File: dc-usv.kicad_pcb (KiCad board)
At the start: 4 copper layers, 120 x 100 mm, 327 parts, among them J1 Output 2.0mm, J10 I2C, J2 Output 2.0mm, J3 Output 2.0mm, J4 SMBUS, J5 HanRun_HR911105A, J6 USB_C_Receptacle_USB2.0, J7 Input 2.0mm, J8 Input 2.5mm, J9 USB_C_Receptacle_USB2.0, Q1 AON7544, Q10 AO4407A, Q11 2N7002, Q12 MMBT3904, Q13 2N7002, Q14 2N7002, Q15 2N7002, Q16 2N7002, Q17 2N7002, Q18 MMBT3904, Q19 AO4407A, Q2 AO3401A, Q20 2N7002, Q21 AO4407A, Q22 2N7002, Q23 AO4407A, Q24 2N7002, Q25 AO3401A, Q26 2N7002, Q28 MMBT3904, Q29 MMBT3904, Q3 AON7544, Q30 MMBT3904, Q31 2N7002, Q32 AO4407A, Q33 MMBT3904, Q34 2N7002, Q35 AO4407A, Q36 MMBT3904, Q37 2N7002, Q38 AO4407A, Q4 AON7544, Q5 AON7544, Q6 CSD17308Q3, Q7 CSD17308Q3, Q8 AO4407A, Q9 2N7002, SW1 SW_DIP_x02, SW2 SW_Push, U1 BQ40z50-R2, U10 LAN8720A, U11 74HC595, U12 SY8105, U13 LM75B, U14 INA219AxD, U15 INA219AxD, U16 CH340G, U17 N066-6448TSWEG03-H28, U18 SRV05-4, U2 LM75B, U3 BQ24715, U4 TPS61178x, U5 INA219AxD, U6 INA219AxD, U7 LM75B, U8 SY8120B1ABC, U9 ESP32-WROOM-32E, Y1 12MHz

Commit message: Add tooling holes
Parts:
- added H1: MountingHole, ToolingHole:ToolingHole_JLCSMT, F.Cu at (21.5, 21.5)
- added H2: MountingHole, ToolingHole:ToolingHole_JLCSMT, F.Cu at (138.5, 118.5)
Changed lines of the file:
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@@
     )
   )
+  (footprint "ToolingHole:ToolingHole_JLCSMT" (layer "F.Cu")
+    (at 21.5 21.5)
+    (property "Sheetfile" "dc-usv.kicad_sch")
+    (property "Sheetname" "")
+    (property "exclude_from_bom" "")
+    (attr through_hole exclude_from_bom)
+    (fp_text reference "H1" (at 0 0.5) (layer "F.SilkS") hide
+      (effects (font (size 1 1) (thickness 0.15)))
+    )
+    (fp_text value "MountingHole" (at 0 -0.5) (layer "F.Fab")
+      (effects (font (size 1 1) (thickness 0.15)))
+    )
+    (fp_text user "tooling hole" (at -6.5 0) (layer "F.SilkS")
+      (effects (font (size 1 1) (thickness 0.15)))
+    )
+    (pad "" np_thru_hole circle locked (at 0 0) (size 1.152 1.152) (drill 1.152) (layers *.Cu *.Mask))
+  )
   (footprint "Resistor_SMD:R_0603_1608Metric" (layer "F.Cu")
     (at 117.75 87.0125 -90)
@@
     )
   )
+  (footprint "ToolingHole:ToolingHole_JLCSMT" (layer "F.Cu")
+    (at 138.5 118.5)
+    (property "Sheetfile" "dc-usv.kicad_sch")
+    (property "Sheetname" "")
+    (property "exclude_from_bom" "")
+    (attr through_hole exclude_from_bom)
+    (fp_text reference "H2" (at 0 0.5) (layer "F.SilkS") hide
+      (effects (font (size 1 1) (thickness 0.15)))
+    )
+    (fp_text value "MountingHole" (at 0 -0.5) (layer "F.Fab")
+      (effects (font (size 1 1) (thickness 0.15)))
+    )
+    (fp_text user "tooling hole" (at 7 0) (layer "F.SilkS")
+      (effects (font (size 1 1) (thickness 0.15)))
+    )
+    (pad "" np_thru_hole circle locked (at 0 0) (size 1.152 1.152) (drill 1.152) (layers *.Cu *.Mask))
+  )
   (footprint "Capacitor_SMD:C_0805_2012Metric" (layer "F.Cu")

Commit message: Add thermal plane to SYSPWR MOSFET
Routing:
- net /Battery Pack/BAT+: vias 31 -> 34
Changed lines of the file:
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@@
   (segment (start 122.925 92.7625) (end 122.675001 92.5125) (width 0.127) (layer "F.Cu") (net 21))
   (segment (start 47.75 113.15) (end 47.75 114.570001) (width 0.5) (layer "F.Cu") (net 21))
+  (via (at 49.625 113.175) (size 0.45) (drill 0.2) (layers "F.Cu" "B.Cu") (free) (net 21))
   (via (at 114.7 98.4) (size 0.45) (drill 0.2) (layers "F.Cu" "B.Cu") (free) (net 21))
   (via (at 48.997702 114.576692) (size 0.45) (drill 0.2) (layers "F.Cu" "B.Cu") (net 21))
@@
   (via (at 79.625 115.725) (size 0.45) (drill 0.2) (layers "F.Cu" "B.Cu") (free) (net 21))
   (via (at 118.725 99.475) (size 0.45) (drill 0.2) (layers "F.Cu" "B.Cu") (net 21))
+  (via (at 48.35 113.15) (size 0.45) (drill 0.2) (layers "F.Cu" "B.Cu") (free) (net 21))
+  (via (at 50.9 113.15) (size 0.45) (drill 0.2) (layers "F.Cu" "B.Cu") (free) (net 21))
   (segment (start 124.325 95.175) (end 123.85 95.65) (width 0.127) (layer "B.Cu") (net 21))
   (segment (start 123.05 95.75) (end 119.6 95.75) (width 0.127) (layer "B.Cu") (net 21))
@@
       )
     )
+  )
+  (zone (net 21) (net_name "/Battery Pack/BAT+") (layer "F.Cu") (hatch edge 0.508)
+    (priority 100)
+    (connect_pads thru_hole_only (clearance 0.127))
+    (min_thickness 0.127) (filled_areas_thickness no)
+    (fill yes (thermal_gap 0.508) (thermal_bridge_width 0.508))
+    (polygon
+      (pts
+        (xy 52.3 115)
+        (xy 47 115)
+        (xy 47 110.2)
+        (xy 52.3 110.2)
+      )
+    )

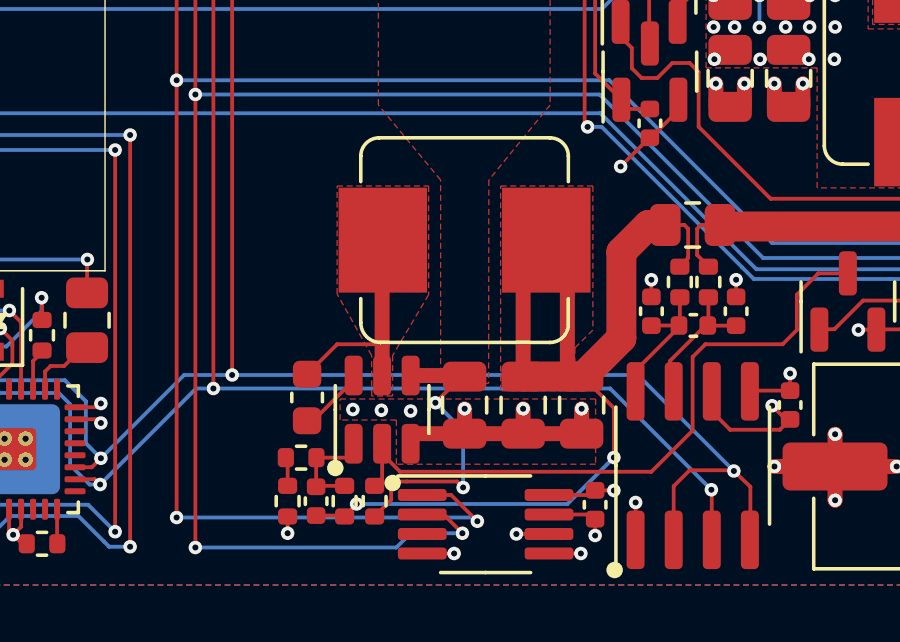
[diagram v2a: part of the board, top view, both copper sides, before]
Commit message: Optimize thermal connectivity of USB output regulator
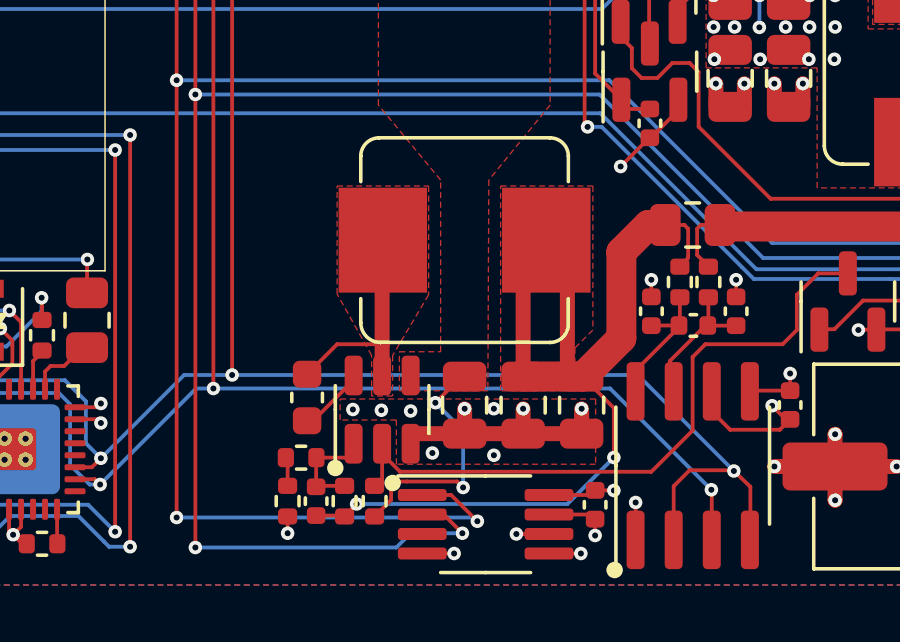
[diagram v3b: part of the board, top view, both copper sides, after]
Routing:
- net /Charger/CS+: track 103.9 -> 102.1 mm
- net GND: vias 239 -> 242
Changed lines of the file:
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@@
   (via (at 41.1 96.025) (size 0.45) (drill 0.2) (layers "F.Cu" "B.Cu") (net 10))
   (via (at 120.8 113.05) (size 0.45) (drill 0.2) (layers "F.Cu" "B.Cu") (net 10))
+  (via (at 107.375 111.125) (size 0.45) (drill 0.2) (layers "F.Cu" "B.Cu") (free) (net 10))
   (via (at 32.2 34.097529) (size 0.45) (drill 0.2) (layers "F.Cu" "B.Cu") (net 10))
   (via (at 82.8 115.825) (size 0.45) (drill 0.2) (layers "F.Cu" "B.Cu") (net 10))
@@
   (via (at 132.775 107.025) (size 0.45) (drill 0.2) (layers "F.Cu" "B.Cu") (net 10))
   (via (at 27.565 33.06) (size 0.45) (drill 0.2) (layers "F.Cu" "B.Cu") (net 10))
+  (via (at 105.325 112.6) (size 0.45) (drill 0.2) (layers "F.Cu" "B.Cu") (free) (net 10))
   (via (at 38 104.975) (size 0.45) (drill 0.2) (layers "F.Cu" "B.Cu") (net 10))
   (via (at 130.234999 91) (size 0.45) (drill 0.2) (layers "F.Cu" "B.Cu") (net 10))
@@
   (via (at 25.95 36.35) (size 0.45) (drill 0.2) (layers "F.Cu" "B.Cu") (net 10))
   (via (at 49.55 71.175) (size 0.45) (drill 0.2) (layers "F.Cu" "B.Cu") (net 10))
+  (via (at 107.375 112.675) (size 0.45) (drill 0.2) (layers "F.Cu" "B.Cu") (free) (net 10))
   (via (at 118.75 94.8625) (size 0.45) (drill 0.2) (layers "F.Cu" "B.Cu") (free) (net 10))
   (via (at 125.525 106.975) (size 0.45) (drill 0.2) (layers "F.Cu" "B.Cu") (net 10))
@@
   (segment (start 50.35 91.4) (end 50.35 89.95) (width 0.127) (layer "F.Cu") (net 19))
   (segment (start 50.575 96.23) (end 50.575 96.225) (width 0.127) (layer "F.Cu") (net 19))
-  (segment (start 104.6 110.0175) (end 106.3925 110.0175) (width 0.5) (layer "F.Cu") (net 19))
   (segment (start 49.3625 98.1) (end 49.725 98.1) (width 0.127) (layer "F.Cu") (net 19))
   (segment (start 106.295 110.055) (end 105.425 110.925) (width 0.127) (layer "F.Cu") (net 19))
@@
         (xy 109.25 101)
         (xy 107.206701 103.500007)
-        (xy 107.2 110.275)
-        (xy 105.6 110.275)
+        (xy 107.175 110.525)
+        (xy 104.225 110.525)
+        (xy 104.225 109.225)
+        (xy 105.6 109.225)
         (xy 105.6 103.5)
         (xy 103.525 101)
